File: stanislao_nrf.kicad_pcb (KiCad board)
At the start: 2 copper layers, 53.5 x 21 mm, 19 parts, among them J1 Conn_01x06, Q1 BTS4140N, Q2 BSP89, U1 NRF52840-DONGLE, U2 LM5007MM

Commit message: Non chinese version
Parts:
- C2: footprint Capacitor_SMD:C_0402_1005Metric -> Capacitor_SMD:C_1206_3216Metric
- R1: footprint Resistor_SMD:R_0402_1005Metric -> Resistor_SMD:R_0603_1608Metric
- moved C2 3.41 mm to (93.0, 68.4), turned to 90 degrees
- moved R1 0.51 mm to (91.8, 73.3)
- moved C3 0.29 mm to (91.3, 72.1)
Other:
- board text added: "BRAKE"
- board text added: "GND"
- board text added: "RX"
- board text added: "TX"
- board text added: "VIN"
- board text added: "V_BATT"

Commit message: Cleanup
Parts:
- added REF**: JST_XH_B2B-XH-A_1x02_P2.50mm_Vertical, Connector_JST:JST_XH_B2B-XH-A_1x02_P2.50mm_Vertical, B.Cu at (90.2, 83.8)
- added REF**: JST_XH_B2B-XH-A_1x02_P2.50mm_Vertical, Connector_JST:JST_XH_B2B-XH-A_1x02_P2.50mm_Vertical, B.Cu at (99.1, 83.8)
- added REF**: JST_XH_B2B-XH-A_1x02_P2.50mm_Vertical, Connector_JST:JST_XH_B2B-XH-A_1x02_P2.50mm_Vertical, B.Cu at (92.7, 57.1)
- added REF**: JST_XH_B2B-XH-A_1x02_P2.50mm_Vertical, Connector_JST:JST_XH_B2B-XH-A_1x02_P2.50mm_Vertical, B.Cu at (101.6, 57.1)
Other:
- board size 53.5 x 21 mm -> 53.7 x 31.8 mm

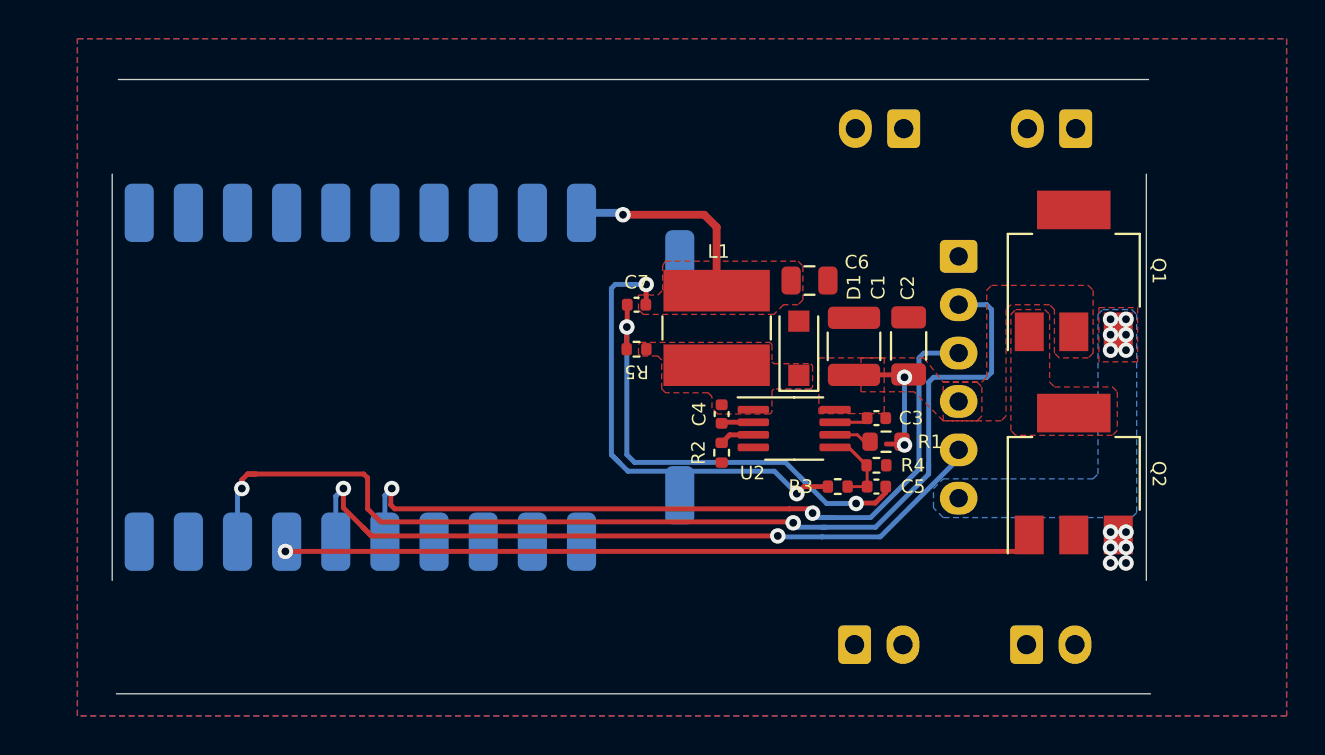
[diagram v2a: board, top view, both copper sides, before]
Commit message: Smol dc/dc
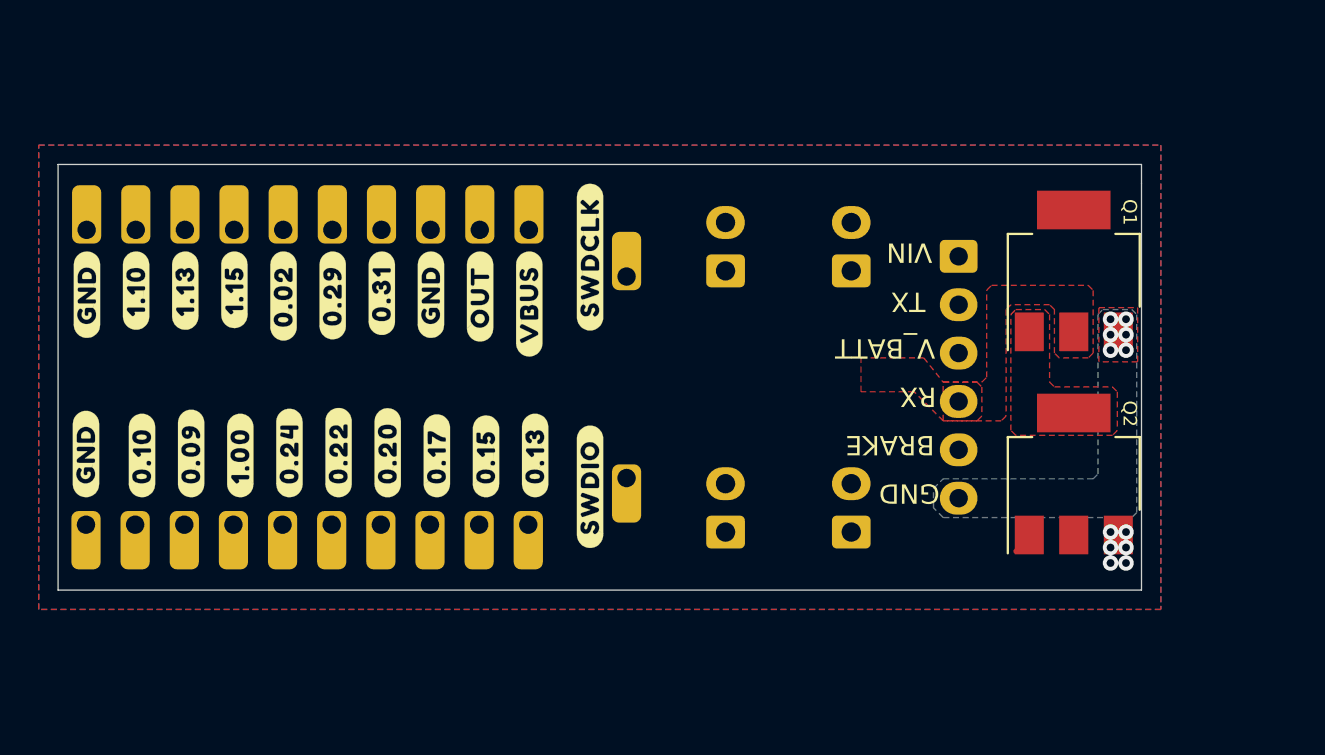
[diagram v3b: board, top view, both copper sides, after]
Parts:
- removed C1: 10uF, Capacitor_SMD:C_1210_3225Metric
- removed C2: 0.1uF, Capacitor_SMD:C_1206_3216Metric
- removed C3, C4, C5: 0.1uF, Capacitor_SMD:C_0402_1005Metric
- removed C6: 10uF, Capacitor_SMD:C_0805_2012Metric
- removed C7: 3nF, Capacitor_SMD:C_0402_1005Metric
- removed D1: D_Schottky_Small, Diode_SMD:D_SOD-123F
- removed L1: 100uH, Inductor_SMD:L_TracoPower_TCK-047_5.2x5.8mm
- removed R1: 127K, Resistor_SMD:R_0603_1608Metric
- removed R2: 278K, Resistor_SMD:R_0402_1005Metric
- removed R3, R4: 1K, Resistor_SMD:R_0402_1005Metric
- removed R5: 100K, Resistor_SMD:R_0402_1005Metric
- removed REF** (x4): JST_XH_B2B-XH-A_1x02_P2.50mm_Vertical, Connector_JST:JST_XH_B2B-XH-A_1x02_P2.50mm_Vertical
- removed U2: LM5007MM, Package_SO:MSOP-8_3x3mm_P0.65mm
- added ?: , buzzardLabel, F.Cu at (65.7, 63.5)
- added ?: , buzzardLabel, F.Cu at (50.5, 63.5)
- added ?: , buzzardLabel, F.Cu at (50.4, 76.2)
- added ?: , buzzardLabel, F.Cu at (55.9, 76.2)
- added ?: , buzzardLabel, F.Cu at (73.7, 76.2)
- added ?: , buzzardLabel, F.Cu at (76.5, 60.0)
- added ?: , buzzardLabel, F.Cu at (66.0, 76.2)
- added ?: , buzzardLabel, F.Cu at (68.6, 76.2)
- added ?: , buzzardLabel, F.Cu at (71.1, 76.2)
- added ?: , buzzardLabel, F.Cu at (70.8, 63.5)
- added ?: , buzzardLabel, F.Cu at (58.4, 76.2)
- added ?: , buzzardLabel, F.Cu at (68.3, 63.5)
- added ?: , buzzardLabel, F.Cu at (61.0, 76.2)
- added ?: , buzzardLabel, F.Cu at (73.4, 63.5)
- added ?: , buzzardLabel, F.Cu at (63.5, 76.2)
- added ?: , buzzardLabel, F.Cu at (60.7, 63.5)
- added ?: , buzzardLabel, F.Cu at (63.2, 63.5)
- added ?: , buzzardLabel, F.Cu at (53.3, 76.2)
- added ?: , buzzardLabel, F.Cu at (58.1, 63.5)
- added ?: , buzzardLabel, F.Cu at (53.0, 63.5)
- added ?: , buzzardLabel, F.Cu at (55.6, 63.5)
- added ?: , buzzardLabel, F.Cu at (76.5, 72.5)
- added J2: Conn_01x02, Connector_JST:JST_XH_B2B-XH-A_1x02_P2.50mm_Vertical, B.Cu at (90.0, 78.0)
- added J3: Conn_01x02, Connector_JST:JST_XH_B2B-XH-A_1x02_P2.50mm_Vertical, B.Cu at (83.5, 78.0)
- added J4: Conn_01x02, Connector_JST:JST_XH_B2B-XH-A_1x02_P2.50mm_Vertical, B.Cu at (90.0, 64.5)
- added J5: Conn_01x02, Connector_JST:JST_XH_B2B-XH-A_1x02_P2.50mm_Vertical, B.Cu at (83.5, 64.5)
- J1: value Conn_01x06 -> JST_HX_S6B
- moved U1 2.75 mm to (67.8, 70.0)
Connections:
- net /BTS414ON_CTRL renamed Net-(Q1-Pad1)
- Q2 pad 1: /P1.00 -> Net-(Q2-Pad1)
- U1 pad 0.02: unconnected-(U1-Pad0.02) -> (no net)
- U1 pad 0.10: unconnected-(U1-Pad0.10) -> (no net)
- U1 pad 0.13: unconnected-(U1-Pad0.13) -> (no net)
- U1 pad 0.15: unconnected-(U1-Pad0.15) -> (no net)
- U1 pad 0.17: unconnected-(U1-Pad0.17) -> (no net)
- U1 pad 0.20: unconnected-(U1-Pad0.20) -> (no net)
- U1 pad 0.29: unconnected-(U1-Pad0.29) -> (no net)
- U1 pad 0.31: unconnected-(U1-Pad0.31) -> (no net)
- U1 pad 1.10: unconnected-(U1-Pad1.10) -> (no net)
- U1 pad 1.13: unconnected-(U1-Pad1.13) -> (no net)
- U1 pad 1.15: unconnected-(U1-Pad1.15) -> (no net)
- U1 pad OUT: unconnected-(U1-PadOUT) -> (no net)
- U1 pad SWDCLK: unconnected-(U1-PadSWDCLK) -> (no net)
- U1 pad SWDIO: unconnected-(U1-PadSWDIO) -> (no net)
- U1 pad VBUS: Net-(C6-Pad1) -> VBUS
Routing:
- net /TSDZ2_BRAKE_INPUT: track 56.3 -> 0.00 mm, vias 2 -> 0
- net /TSDZ2_RX: track 40.8 -> 0.00 mm, vias 2 -> 0
- net /P1.00: track 39.5 -> 0.00 mm, vias 1 -> 0
- net /TSDZ2_TX: track 39.1 -> 0.52 mm, vias 2 -> 0
- net Net-(C6-Pad1): track 34.9 -> 0.00 mm, vias 3 -> 0
- net Net-(C5-Pad1): track 24.6 -> 0.00 mm, vias 2 -> 0
- net /V_BATT: track 7.12 -> 0.00 mm, vias 2 -> 0
- net Net-(C5-Pad2): track 5.49 -> 0.00 mm
- net Net-(R1-Pad2): track 1.82 -> 0.00 mm
- net Net-(R2-Pad1): track 1.81 -> 0.00 mm
- net Net-(C3-Pad2): track 1.75 -> 0.00 mm
- net Net-(C4-Pad1): track 1.66 -> 0.00 mm
- net Net-(Q2-Pad1): track 0.00 -> 1.14 mm
- added copper zone on F.Cu, net /TSDZ2_RX
- removed copper zone on F.Cu, net Net-(C4-Pad2)
- removed copper zone on F.Cu, net Net-(C6-Pad1)
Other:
- board size 53.7 x 31.8 mm -> 56 x 22 mm

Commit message: Awaiting for logo
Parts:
- removed the ? at (50.5, 63.5)
- removed the ? at (50.4, 76.2)
- removed the ? at (70.8, 63.5)
- removed the ? at (68.3, 63.5)
- removed the ? at (73.4, 63.5)
- removed J2, J3, J4, J5: Conn_01x02, Connector_JST:JST_XH_B2B-XH-A_1x02_P2.50mm_Vertical
- removed Q2: BSP89, Package_TO_SOT_SMD:SOT-223-3_TabPin2
- added ?: , buzzardLabel, F.Cu at (94.2, 71.2)
- added ?: , buzzardLabel, F.Cu at (82.2, 75.5)
- added ?: , buzzardLabel, F.Cu at (82.4, 64.5)
- added ?: , buzzardLabel, F.Cu at (50.5, 63.0)
- added ?: , buzzardLabel, F.Cu at (94.2, 68.8)
- added ?: , buzzardLabel, F.Cu at (68.3, 63.0)
- added ?: , buzzardLabel, F.Cu at (94.2, 73.8)
- added ?: , buzzardLabel, F.Cu at (88.8, 62.0)
- added ?: , buzzardLabel, F.Cu at (50.4, 77.0)
- added ?: , buzzardLabel, F.Cu at (88.9, 64.5)
- added ?: , buzzardLabel, F.Cu at (82.2, 62.0)
- added ?: , buzzardLabel, F.Cu at (94.2, 66.2)
- added ?: , buzzardLabel, F.Cu at (73.4, 63.3)
- added ?: , buzzardLabel, F.Cu at (94.5, 63.8)
- added ?: , buzzardLabel, F.Cu at (94.2, 76.2)
- added ?: , buzzardLabel, F.Cu at (70.8, 63.3)
- added ?: , buzzardLabel, F.Cu at (82.4, 78.0)
- added ?: , buzzardLabel, F.Cu at (88.9, 78.0)
- added ?: , buzzardLabel, B.Cu at (52.0, 70.0)
- added ?: , buzzardLabel, F.Cu at (88.8, 75.5)
- added C1: 2.2uF, Capacitor_SMD:C_1210_3225Metric, B.Cu at (86.6, 70.2)
- added C6: 22uF, Capacitor_SMD:C_0805_2012Metric, B.Cu at (80.0, 70.0)
- added R6: DNP/100KOhm, Resistor_SMD:R_0603_1608Metric, B.Cu at (92.2, 71.0)
- added REF**: MountingHole_3.2mm_M3, MountingHole:MountingHole_3.2mm_M3, F.Cu at (101.5, 62.5)
- added REF**: MountingHole_3.2mm_M3, MountingHole:MountingHole_3.2mm_M3, F.Cu at (101.5, 77.5)
- added SW1: SW_Push, Connector_JST:JST_XH_B2B-XH-A_1x02_P2.50mm_Vertical, B.Cu at (90.0, 78.0)
- added SW2: SW_Push, Connector_JST:JST_XH_B2B-XH-A_1x02_P2.50mm_Vertical, B.Cu at (90.0, 64.5)
- added SW3: SW_Push, Connector_JST:JST_XH_B2B-XH-A_1x02_P2.50mm_Vertical, B.Cu at (83.6, 78.0)
- added SW4: SW_Push, Connector_JST:JST_XH_B2B-XH-A_1x02_P2.50mm_Vertical, B.Cu at (83.6, 64.5)
- added U2: TPSM265R1, stanislao_nrf-backups:TPSM265R1, B.Cu at (83.0, 70.0)
- Q1: value BTS4140N -> SSM6J507NU; footprint Package_TO_SOT_SMD:SOT-223-3_TabPin2 -> footprints:UDFN6B; moved to B.Cu
- moved Q1 13.3 mm to (90.0, 71.2), turned to 180 degrees
- moved ? 0.62 mm to (65.7, 76.7)
- moved ? 0.62 mm to (70.8, 76.7)
- moved ? 0.62 mm to (55.5, 76.7)
- moved ? 0.62 mm to (58.1, 76.7)
- moved ? 0.62 mm to (60.6, 76.7)
- moved ? 0.62 mm to (63.1, 76.7)
- moved ? 0.62 mm to (53.0, 76.7)
- moved ? 0.62 mm to (73.3, 76.7)
- moved ? 0.62 mm to (68.2, 76.7)
- moved ? 0.20 mm to (65.7, 63.3)
- moved ? 0.20 mm to (55.6, 63.3)
- moved ? 0.20 mm to (60.7, 63.3)
- moved ? 0.20 mm to (63.2, 63.3)
- moved ? 0.20 mm to (58.1, 63.3)
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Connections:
- Q1 pad 1: Net-(Q1-Pad1) -> /V_BATT
- Q1 pad 3: /TSDZ2_VIN -> /P1.00_VIN_CTRL
- U1 pad 0.13: (no net) -> /P0.13_UP
- U1 pad 0.15: (no net) -> /P0.15_ENTER
- U1 pad 0.17: (no net) -> /P0.17_DOWN
- U1 pad 0.20: (no net) -> /P0.20_POWER
- U1 pad 1.00: /P1.00 -> /P1.00_VIN_CTRL
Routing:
- net /TSDZ2_RX: track 0.00 -> 69.1 mm
- net /TSDZ2_BRAKE_INPUT: track 0.00 -> 50.4 mm
- net /P1.00_VIN_CTRL: track 0.00 -> 44.3 mm, vias 0 -> 2
- net /TSDZ2_TX: track 0.52 -> 43.7 mm, vias 0 -> 1
- net /P0.17_DOWN: track 0.00 -> 41.9 mm, vias 0 -> 1
- net /P0.20_POWER: track 0.00 -> 34.8 mm, vias 0 -> 1
- net /V_BATT: track 0.00 -> 30.0 mm, vias 0 -> 2
- net GND: track 0.00 -> 27.1 mm, vias 6 -> 0
- net VBUS: track 0.00 -> 21.5 mm, vias 0 -> 2
- net /P0.13_UP: track 0.00 -> 19.3 mm
- net /P0.15_ENTER: track 0.00 -> 16.1 mm
- net /TSDZ2_VIN: track 0.00 -> 8.76 mm, vias 6 -> 0
- net Net-(Q2-Pad1): track 1.14 -> 0.00 mm
- removed copper zone on F.Cu, net /TSDZ2_RX
- removed copper zone on B.Cu, net /TSDZ2_VIN
- removed copper zone on F.Cu, net /TSDZ2_VIN
- removed copper zone on F.Cu, net /V_BATT
- removed copper zone on F.Cu, net Net-(Q1-Pad1)
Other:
- board text removed: "BRAKE"
- board text removed: "GND"
- board text removed: "RX"
- board text removed: "TX"
- board text removed: "VIN"
- board text removed: "V_BATT"
